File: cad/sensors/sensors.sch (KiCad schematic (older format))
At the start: 75 parts, among them J1 Conn_01x04, J2 Conn_01x04, J3 6P6C, J4 Conn_01x04, J5 Conn_01x04, J6 Conn_01x04, J7 Conn_01x02, U1 LMV324, U2 PCA9517A, U3 LMV331, U4 MC14040B, U5 MC14040B, U6 TCA9555DBR, U7 PCF8574

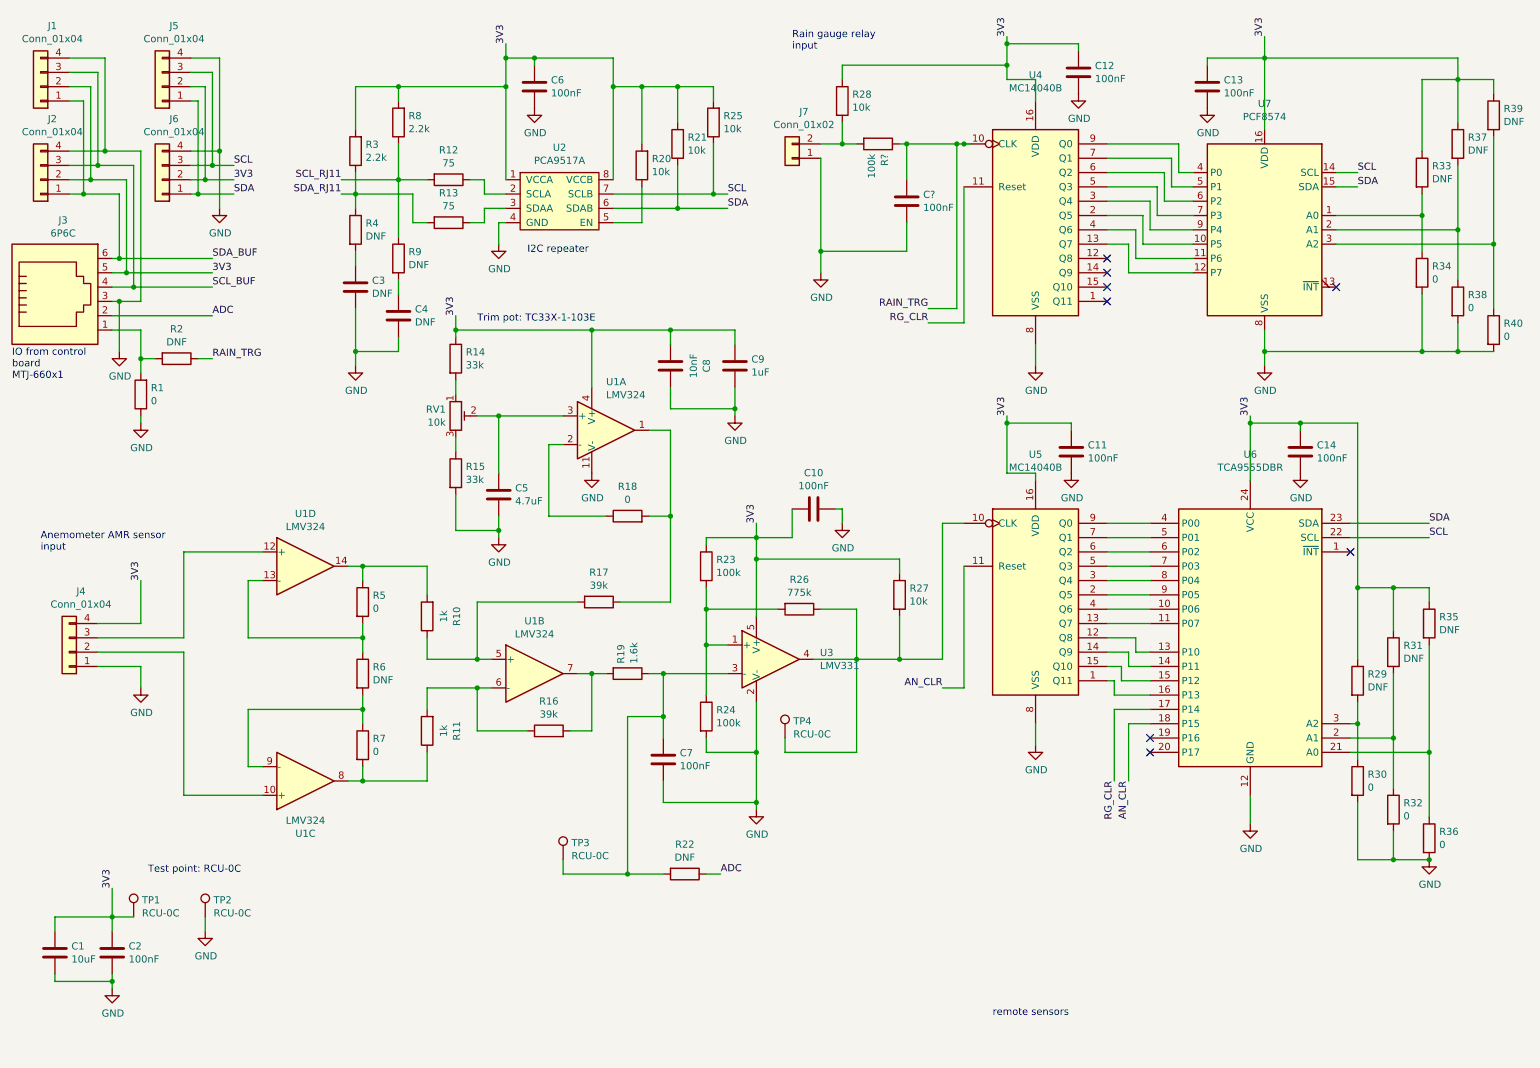
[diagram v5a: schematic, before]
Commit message: Defined sensor board outline. Began assigning footprints
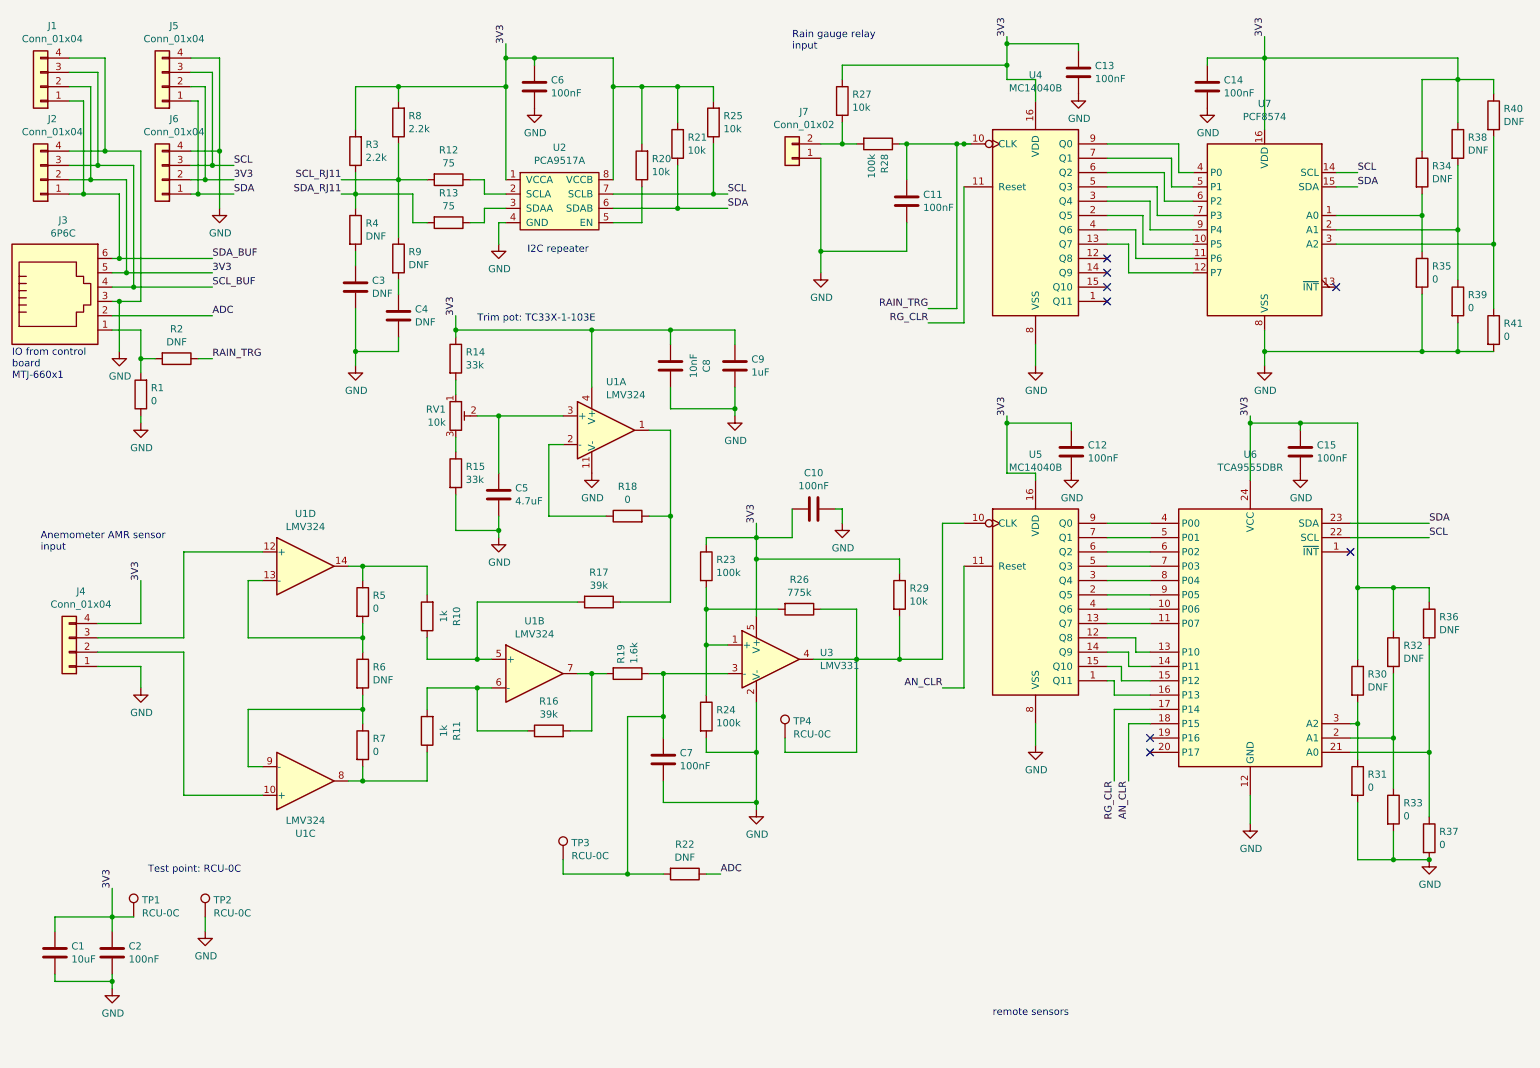
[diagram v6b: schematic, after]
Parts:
- gave numbers to parts that had none: 2
- renumbered C11 to C12, C12 to C13, C13 to C14, C14 to C15, R28 to R27, R27 to R29, R29 to R30, R30 to R31, R31 to R32, R32 to R33, R33 to R34, R34 to R35, R35 to R36, R36 to R37, R37 to R38, R38 to R39, R39 to R40, R40 to R41
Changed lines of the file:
@@
 	7700 3700 7700 3750
 $Comp
-L Device:R R27
+L Device:R R29
 U 1 1 62C3B7EE
 P 6750 4550
-F 0 "R27" H 6820 4596 50  0000 L CNN
+F 0 "R29" H 6820 4596 50  0000 L CNN
 F 1 "10k" H 6820 4505 50  0000 L CNN
 F 2 "Resistor_SMD:R_0603_1608Metric" V 6680 4550 50  0001 C CNN
@@
 $EndComp
 $Comp
-L power:GND #PWR015
+L power:GND #PWR014
 U 1 1 62326995
 P 6200 2300
-F 0 "#PWR015" H 6200 2050 50  0001 C CNN
+F 0 "#PWR014" H 6200 2050 50  0001 C CNN
 F 1 "GND" H 6205 2127 50  0000 C CNN
 F 2 "" H 6200 2300 50  0001 C CNN
@@
 $EndComp
 $Comp
-L Device:R R28
+L Device:R R27
 U 1 1 6232699B
 P 6350 1100
-F 0 "R28" H 6420 1146 50  0000 L CNN
+F 0 "R27" H 6420 1146 50  0000 L CNN
 F 1 "10k" H 6420 1055 50  0000 L CNN
 F 2 "Resistor_SMD:R_0603_1608Metric" V 6280 1100 50  0001 C CNN
@@
 	6350 3950 6350 4050
 $Comp
-L power:GND #PWR014
+L power:GND #PWR015
 U 1 1 626A554D
 P 6350 4050
-F 0 "#PWR014" H 6350 3800 50  0001 C CNN
+F 0 "#PWR015" H 6350 3800 50  0001 C CNN
 F 1 "GND" H 6355 3877 50  0000 C CNN
 F 2 "" H 6350 4050 50  0001 C CNN
@@
 Connection ~ 2000 1450
 $Comp
-L Device:R R29
+L Device:R R30
 U 1 1 62411B40
 P 9950 5150
-F 0 "R29" H 10020 5196 50  0000 L CNN
+F 0 "R30" H 10020 5196 50  0000 L CNN
 F 1 "DNF" H 10020 5105 50  0000 L CNN
 F 2 "Resistor_SMD:R_0603_1608Metric" V 9880 5150 50  0001 C CNN
@@
 $EndComp
 $Comp
-L Device:R R31
+L Device:R R32
 U 1 1 6242B925
 P 10200 4950
-F 0 "R31" H 10270 4996 50  0000 L CNN
+F 0 "R32" H 10270 4996 50  0000 L CNN
 F 1 "DNF" H 10270 4905 50  0000 L CNN
 F 2 "Resistor_SMD:R_0603_1608Metric" V 10130 4950 50  0001 C CNN
@@
 $EndComp
 $Comp
-L Device:R R35
+L Device:R R36
 U 1 1 62443EB2
 P 10450 4750
-F 0 "R35" H 10520 4796 50  0000 L CNN
+F 0 "R36" H 10520 4796 50  0000 L CNN
 F 1 "DNF" H 10520 4705 50  0000 L CNN
 F 2 "Resistor_SMD:R_0603_1608Metric" V 10380 4750 50  0001 C CNN
@@
 	9950 4500 9950 5000
 $Comp
-L Device:R R36
+L Device:R R37
 U 1 1 62530694
 P 10450 6250
-F 0 "R36" H 10520 6296 50  0000 L CNN
+F 0 "R37" H 10520 6296 50  0000 L CNN
 F 1 "0" H 10520 6205 50  0000 L CNN
 F 2 "Resistor_SMD:R_0603_1608Metric" V 10380 6250 50  0001 C CNN
@@
 $EndComp
 $Comp
-L Device:R R32
+L Device:R R33
 U 1 1 6254A7B7
 P 10200 6050
-F 0 "R32" H 10270 6096 50  0000 L CNN
+F 0 "R33" H 10270 6096 50  0000 L CNN
 F 1 "0" H 10270 6005 50  0000 L CNN
 F 2 "Resistor_SMD:R_0603_1608Metric" V 10130 6050 50  0001 C CNN
@@
 $EndComp
 $Comp
-L Device:R R30
+L Device:R R31
 U 1 1 62562994
 P 9950 5850
-F 0 "R30" H 10020 5896 50  0000 L CNN
+F 0 "R31" H 10020 5896 50  0000 L CNN
 F 1 "0" H 10020 5805 50  0000 L CNN
 F 2 "Resistor_SMD:R_0603_1608Metric" V 9880 5850 50  0001 C CNN
@@
 	7700 950  7700 1100
 $Comp
-L Device:C C14
+L Device:C C15
 U 1 1 628D9C56
 P 9550 3550
-F 0 "C14" H 9435 3504 50  0000 R CNN
+F 0 "C15" H 9435 3504 50  0000 R CNN
 F 1 "100nF" H 9435 3595 50  0000 R CNN
 F 2 "Capacitor_SMD:C_0603_1608Metric" H 9588 3400 50  0001 C CNN
@@
 	7500 3300 7500 3350
 $Comp
-L Device:C C11
+L Device:C C12
 U 1 1 6297A007
 P 7950 3550
-F 0 "C11" H 7835 3504 50  0000 R CNN
+F 0 "C12" H 7835 3504 50  0000 R CNN
 F 1 "100nF" H 7835 3595 50  0000 R CNN
 F 2 "Capacitor_SMD:C_0603_1608Metric" H 7988 3400 50  0001 C CNN
@@
 3V3
 $Comp
-L Device:C C13
+L Device:C C14
 U 1 1 62A4CA74
 P 8900 1000
-F 0 "C13" H 8785 954 50  0000 R CNN
+F 0 "C14" H 8785 954 50  0000 R CNN
 F 1 "100nF" H 8785 1045 50  0000 R CNN
 F 2 "Capacitor_SMD:C_0603_1608Metric" H 8938 850 50  0001 C CNN
@@
 	9300 800  9300 650
 $Comp
-L Device:C C12
+L Device:C C13
 U 1 1 62AED9B9
 P 8000 900
-F 0 "C12" H 7885 854 50  0000 R CNN
+F 0 "C13" H 7885 854 50  0000 R CNN
 F 1 "100nF" H 7885 945 50  0000 R CNN
 F 2 "Capacitor_SMD:C_0603_1608Metric" H 8038 750 50  0001 C CNN
@@
 	10650 2650 10650 2850
 $Comp
-L Device:R R34
+L Device:R R35
 U 1 1 626D56FC
 P 10400 2300
-F 0 "R34" H 10470 2346 50  0000 L CNN
+F 0 "R35" H 10470 2346 50  0000 L CNN
 F 1 "0" H 10470 2255 50  0000 L CNN
 F 2 "Resistor_SMD:R_0603_1608Metric" V 10330 2300 50  0001 C CNN
@@
 $EndComp
 $Comp
-L Device:R R38
+L Device:R R39
 U 1 1 626D56F6
 P 10650 2500
-F 0 "R38" H 10720 2546 50  0000 L CNN
+F 0 "R39" H 10720 2546 50  0000 L CNN
 F 1 "0" H 10720 2455 50  0000 L CNN
 F 2 "Resistor_SMD:R_0603_1608Metric" V 10580 2500 50  0001 C CNN
@@
 $EndComp
 $Comp
-L Device:R R40
+L Device:R R41
 U 1 1 626D56F0
 P 10900 2700
-F 0 "R40" H 10970 2746 50  0000 L CNN
+F 0 "R41" H 10970 2746 50  0000 L CNN
 F 1 "0" H 10970 2655 50  0000 L CNN
 F 2 "Resistor_SMD:R_0603_1608Metric" V 10830 2700 50  0001 C CNN
@@
 $EndComp
 $Comp
-L Device:R R39
+L Device:R R40
 U 1 1 626D56DC
 P 10900 1200
-F 0 "R39" H 10970 1246 50  0000 L CNN
+F 0 "R40" H 10970 1246 50  0000 L CNN
 F 1 "DNF" H 10970 1155 50  0000 L CNN
 F 2 "Resistor_SMD:R_0603_1608Metric" V 10830 1200 50  0001 C CNN
@@
 $EndComp
 $Comp
-L Device:R R37
+L Device:R R38
 U 1 1 626D56D6
 P 10650 1400
-F 0 "R37" H 10720 1446 50  0000 L CNN
+F 0 "R38" H 10720 1446 50  0000 L CNN
 F 1 "DNF" H 10720 1355 50  0000 L CNN
 F 2 "Resistor_SMD:R_0603_1608Metric" V 10580 1400 50  0001 C CNN
@@
 $EndComp
 $Comp
-L Device:R R33
+L Device:R R34
 U 1 1 626D56D0
 P 10400 1600
-F 0 "R33" H 10470 1646 50  0000 L CNN
+F 0 "R34" H 10470 1646 50  0000 L CNN
 F 1 "DNF" H 10470 1555 50  0000 L CNN
 F 2 "Resistor_SMD:R_0603_1608Metric" V 10330 1600 50  0001 C CNN
@@
 	5150 3100 5150 3250
 $Comp
-L Device:R R?
+L Device:R R28
 U 1 1 625AA245
 P 6600 1400
-F 0 "R?" H 6670 1446 50  0000 L CNN
+F 0 "R28" H 6670 1446 50  0000 L CNN
 F 1 "100k" H 6670 1355 50  0000 L CNN
 F 2 "Resistor_SMD:R_0603_1608Metric" V 6530 1400 50  0001 C CNN
@@
 	6200 1400 6350 1400
 $Comp
-L Device:C C?
+L Device:C C11
 U 1 1 6268216E
 P 6800 1800
-F 0 "C?" H 6685 1754 50  0000 R CNN
+F 0 "C11" H 6685 1754 50  0000 R CNN
 F 1 "100nF" H 6685 1845 50  0000 R CNN
 F 2 "Capacitor_SMD:C_0603_1608Metric" H 6838 1650 50  0001 C CNN

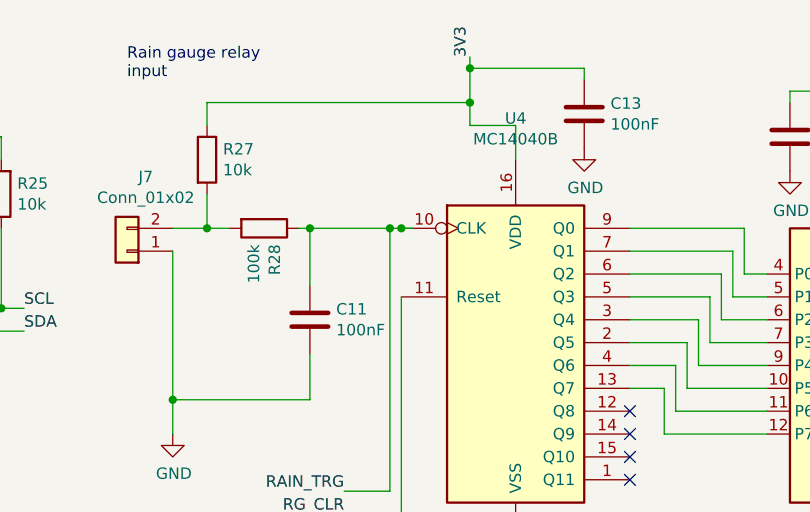
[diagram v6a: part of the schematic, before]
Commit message: Finished sensor breakout board placement. Ready to begin routing
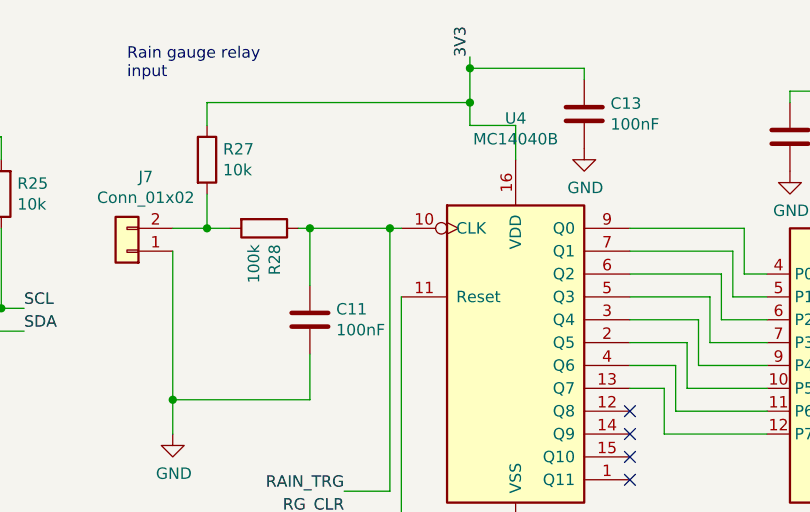
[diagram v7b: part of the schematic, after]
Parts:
- J1, J2, J4, J5, J6: footprint (none) -> Connector_Molex:Molex_KK-254_AE-6410-04A_1x04_P2.54mm_Vertical
- J3: footprint (none) -> custom:E5566-Q0LK22-L
- J7: footprint (none) -> Connector_Molex:Molex_KK-254_AE-6410-02A_1x02_P2.54mm_Vertical
- RV1: footprint (none) -> Potentiometer_SMD:Potentiometer_Bourns_TC33X_Vertical
- TP1, TP2, TP3, TP4: footprint (none) -> TestPoint:TestPoint_Pad_2.0x2.0mm
- U1: footprint (none) -> Package_SO:TSSOP-14_4.4x5mm_P0.65mm
- U2: footprint (none) -> Package_SO:TSSOP-8_3x3mm_P0.65mm
- U3: footprint (none) -> Package_SO:TSOP-5_1.65x3.05mm_P0.95mm
- U4, U5: footprint (none) -> Package_SO:SOIC-16_3.9x9.9mm_P1.27mm
- U7: footprint (none) -> Package_SO:SOIC-16W_7.5x10.3mm_P1.27mm
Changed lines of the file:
@@
 F 0 "J3" H 907 3067 50  0000 C CNN
 F 1 "6P6C" H 907 2976 50  0000 C CNN
-F 2 "" V 850 2525 50  0001 C CNN
+F 2 "custom:E5566-Q0LK22-L" V 850 2525 50  0001 C CNN
 F 3 "~" V 850 2525 50  0001 C CNN
 	1    850  2500
@@
 F 0 "U5" H 7700 5531 50  0000 C CNN
 F 1 "MC14040B" H 7700 5440 50  0000 C CNN
-F 2 "" H 7700 4550 50  0001 C CNN
+F 2 "Package_SO:SOIC-16_3.9x9.9mm_P1.27mm" H 7700 4550 50  0001 C CNN
 F 3 "http://www.intersil.com/content/dam/Intersil/documents/cd40/cd4020bms-24bms-40bms.pdf" H 7700 4550 50  0001 C CNN
 	1    7700 4550
@@
 F 0 "U4" H 7700 2881 50  0000 C CNN
 F 1 "MC14040B" H 7700 2790 50  0000 C CNN
-F 2 "" H 7700 1900 50  0001 C CNN
+F 2 "Package_SO:SOIC-16_3.9x9.9mm_P1.27mm" H 7700 1900 50  0001 C CNN
 F 3 "http://www.intersil.com/content/dam/Intersil/documents/cd40/cd4020bms-24bms-40bms.pdf" H 7700 1900 50  0001 C CNN
 	1    7700 1900
@@
 F 0 "J7" H 5918 1175 50  0000 C CNN
 F 1 "Conn_01x02" H 5918 1266 50  0000 C CNN
-F 2 "" H 6000 1500 50  0001 C CNN
+F 2 "Connector_Molex:Molex_KK-254_AE-6410-02A_1x02_P2.54mm_Vertical" H 6000 1500 50  0001 C CNN
 F 3 "~" H 6000 1500 50  0001 C CNN
 	1    6000 1500
@@
 	8250 5350 8500 5350
 Wire Wire Line
-	7200 1400 7250 1400
-Wire Wire Line
 	8200 2100 8350 2100
 Wire Wire Line
@@
 F 0 "U7" H 9300 2881 50  0000 C CNN
 F 1 "PCF8574" H 9300 2790 50  0000 C CNN
-F 2 "" H 9300 2000 50  0001 C CNN
+F 2 "Package_SO:SOIC-16W_7.5x10.3mm_P1.27mm" H 9300 2000 50  0001 C CNN
 F 3 "http://www.nxp.com/documents/data_sheet/PCF8574_PCF8574A.pdf" H 9300 2000 50  0001 C CNN
 	1    9300 2000
@@
 F 0 "U3" H 6194 5046 50  0000 L CNN
 F 1 "LMV331" H 6194 4955 50  0000 L CNN
-F 2 "" H 5850 5100 50  0001 C CNN
+F 2 "Package_SO:TSOP-5_1.65x3.05mm_P0.95mm" H 5850 5100 50  0001 C CNN
 F 3 "http://www.ti.com/lit/ds/symlink/lmv331.pdf" H 5850 5200 50  0001 C CNN
 	1    5850 5000
@@
 F 0 "J4" H 868 4525 50  0000 C CNN
 F 1 "Conn_01x04" H 868 4616 50  0000 C CNN
-F 2 "" H 950 4950 50  0001 C CNN
+F 2 "Connector_Molex:Molex_KK-254_AE-6410-04A_1x04_P2.54mm_Vertical" H 950 4950 50  0001 C CNN
 F 3 "~" H 950 4950 50  0001 C CNN
 	1    950  4950
@@
 F 0 "J2" H 668 1225 50  0000 C CNN
 F 1 "Conn_01x04" H 668 1316 50  0000 C CNN
-F 2 "" H 750 1650 50  0001 C CNN
+F 2 "Connector_Molex:Molex_KK-254_AE-6410-04A_1x04_P2.54mm_Vertical" H 750 1650 50  0001 C CNN
 F 3 "~" H 750 1650 50  0001 C CNN
 	1    750  1650
@@
 F 0 "TP4" H 6008 5668 50  0000 L CNN
 F 1 "RCU-0C" H 6008 5577 50  0000 L CNN
-F 2 "" H 6150 5550 50  0001 C CNN
+F 2 "TestPoint:TestPoint_Pad_2.0x2.0mm" H 6150 5550 50  0001 C CNN
 F 3 "~" H 6150 5550 50  0001 C CNN
 	1    5950 5550
@@
 F 0 "J6" H 1518 1225 50  0000 C CNN
 F 1 "Conn_01x04" H 1518 1316 50  0000 C CNN
-F 2 "" H 1600 1650 50  0001 C CNN
+F 2 "Connector_Molex:Molex_KK-254_AE-6410-04A_1x04_P2.54mm_Vertical" H 1600 1650 50  0001 C CNN
 F 3 "~" H 1600 1650 50  0001 C CNN
 	1    1600 1650
@@
 F 0 "J1" H 668 575 50  0000 C CNN
 F 1 "Conn_01x04" H 668 666 50  0000 C CNN
-F 2 "" H 750 1000 50  0001 C CNN
+F 2 "Connector_Molex:Molex_KK-254_AE-6410-04A_1x04_P2.54mm_Vertical" H 750 1000 50  0001 C CNN
 F 3 "~" H 750 1000 50  0001 C CNN
 	1    750  1000
@@
 F 0 "J5" H 1518 575 50  0000 C CNN
 F 1 "Conn_01x04" H 1518 666 50  0000 C CNN
-F 2 "" H 1600 1000 50  0001 C CNN
+F 2 "Connector_Molex:Molex_KK-254_AE-6410-04A_1x04_P2.54mm_Vertical" H 1600 1000 50  0001 C CNN
 F 3 "~" H 1600 1000 50  0001 C CNN
 	1    1600 1000
@@
 F 0 "U1" H 4658 3446 50  0001 L CNN
 F 1 "LMV324" H 4658 3355 50  0001 L CNN
-F 2 "" H 4650 3500 50  0001 C CNN
+F 2 "Package_SO:TSSOP-14_4.4x5mm_P0.65mm" H 4650 3500 50  0001 C CNN
 F 3 "http://www.ti.com/lit/ds/symlink/lmv324.pdf" H 4750 3600 50  0001 C CNN
 	5    4700 3400
@@
 F 0 "U1" H 2600 4717 50  0000 C CNN
 F 1 "LMV324" H 2600 4626 50  0000 C CNN
-F 2 "" H 2550 4450 50  0001 C CNN
+F 2 "Package_SO:TSSOP-14_4.4x5mm_P0.65mm" H 2550 4450 50  0001 C CNN
 F 3 "http://www.ti.com/lit/ds/symlink/lmv324.pdf" H 2650 4550 50  0001 C CNN
 	4    2600 4350
@@
 F 0 "U1" H 2600 6217 50  0000 C CNN
 F 1 "LMV324" H 2600 6126 50  0000 C CNN
-F 2 "" H 2550 5950 50  0001 C CNN
+F 2 "Package_SO:TSSOP-14_4.4x5mm_P0.65mm" H 2550 5950 50  0001 C CNN
 F 3 "http://www.ti.com/lit/ds/symlink/lmv324.pdf" H 2650 6050 50  0001 C CNN
 	3    2600 5850
@@
 F 0 "U1" H 4700 3767 50  0000 L TNN
 F 1 "LMV324" H 4700 3676 50  0000 L TNN
-F 2 "" H 4650 3500 50  0001 C CNN
+F 2 "Package_SO:TSSOP-14_4.4x5mm_P0.65mm" H 4650 3500 50  0001 C CNN
 F 3 "http://www.ti.com/lit/ds/symlink/lmv324.pdf" H 4750 3600 50  0001 C CNN
 	1    4700 3400
@@
 F 0 "RV1" H 3580 3346 50  0000 R CNN
 F 1 "10k" H 3580 3255 50  0000 R CNN
-F 2 "" H 3650 3300 50  0001 C CNN
+F 2 "Potentiometer_SMD:Potentiometer_Bourns_TC33X_Vertical" H 3650 3300 50  0001 C CNN
 F 3 "~" H 3650 3300 50  0001 C CNN
 	1    3650 3300
@@
 F 0 "TP1" H 1458 6918 50  0000 L CNN
 F 1 "RCU-0C" H 1458 6827 50  0000 L CNN
-F 2 "" H 1600 6800 50  0001 C CNN
+F 2 "TestPoint:TestPoint_Pad_2.0x2.0mm" H 1600 6800 50  0001 C CNN
 F 3 "~" H 1600 6800 50  0001 C CNN
 	1    1400 6800
@@
 F 0 "TP2" H 1958 6918 50  0000 L CNN
 F 1 "RCU-0C" H 1958 6827 50  0000 L CNN
-F 2 "" H 2100 6800 50  0001 C CNN
+F 2 "TestPoint:TestPoint_Pad_2.0x2.0mm" H 2100 6800 50  0001 C CNN
 F 3 "~" H 2100 6800 50  0001 C CNN
 	1    1900 6800
@@
 F 0 "TP3" H 4458 6518 50  0000 L CNN
 F 1 "RCU-0C" H 4458 6427 50  0000 L CNN
-F 2 "" H 4600 6400 50  0001 C CNN
+F 2 "TestPoint:TestPoint_Pad_2.0x2.0mm" H 4600 6400 50  0001 C CNN
 F 3 "~" H 4600 6400 50  0001 C CNN
 	1    4400 6400
@@
 F 0 "U1" H 4200 5467 50  0000 C CNN
 F 1 "LMV324" H 4200 5376 50  0000 C CNN
-F 2 "" H 4150 5200 50  0001 C CNN
+F 2 "Package_SO:TSSOP-14_4.4x5mm_P0.65mm" H 4150 5200 50  0001 C CNN
 F 3 "http://www.ti.com/lit/ds/symlink/lmv324.pdf" H 4250 5300 50  0001 C CNN
 	2    4200 5100
@@
 F 0 "U2" H 4375 1575 50  0000 C CNN
 F 1 "PCA9517A" H 4375 1484 50  0000 C CNN
-F 2 "" H 4400 1500 50  0001 C CNN
+F 2 "Package_SO:TSSOP-8_3x3mm_P0.65mm" H 4400 1500 50  0001 C CNN
 F 3 "" H 4400 1500 50  0001 C CNN
 	1    4400 1500
@@
 	0    1    1    0
 $EndComp
-Connection ~ 7200 1400
 Wire Wire Line
 	6200 1400 6350 1400
@@
 Wire Wire Line
 	7150 2550 7150 1400
+Wire Wire Line
+	6800 1400 7150 1400
+Wire Wire Line
+	6950 2550 7150 2550
+Wire Wire Line
+	7150 1400 7200 1400
 Connection ~ 7150 1400
-Wire Wire Line
-	7150 1400 7200 1400
-Wire Wire Line
-	6800 1400 7150 1400
-Wire Wire Line
-	6950 2550 7150 2550
 $EndSCHEMATC
